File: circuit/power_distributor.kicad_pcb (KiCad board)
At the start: 4 copper layers, 210 x 100 mm, 199 parts, among them J1 UART, J10 AMASS XT60, J11 AMASS XT60, J12 AMASS XT60, J13 AMASS XT60, J14 AMASS XT60, J15 AMASS XT60, J16 AMASS XT60, J17 AMASS XT60, J18 AMASS XT60, J19 USB_B_Mini, J2 Opto_AUX, J3 AMASS XT60, J4 AMASS XT60, J5 AMASS XT60, J6 AMASS XT60, J7 AMASS XT60, J8 AMASS XT60, J9 AMASS XT60, Q1 AUIRFS8409-7P, Q2 IPB009N03LG, Q3 IPB009N03L_G, Q4 AUIRFS8409-7P, Q5 AUIRFS8409-7P, Q6 AUIRFS8409-7P, U1 UWE-12-10-Q12PB-C, U10 FT230XS, U11 MIC5504-3.3YM5, U12 74AHC595D, U13 PS2801C-4, U14 PS2801C-4, U15 LM5060, U16 LM5060, U17 LM5060, U2 UWE-12-10-Q12PB-C, U3 UEI30-050-Q12P-C, U4 TMR_6-2415WI, U5 i6A4W020A033V-001-R, U6 i6A4W020A033V-001-R, U7 LM5060, U8 LM5050-1, U9 LM5050-1

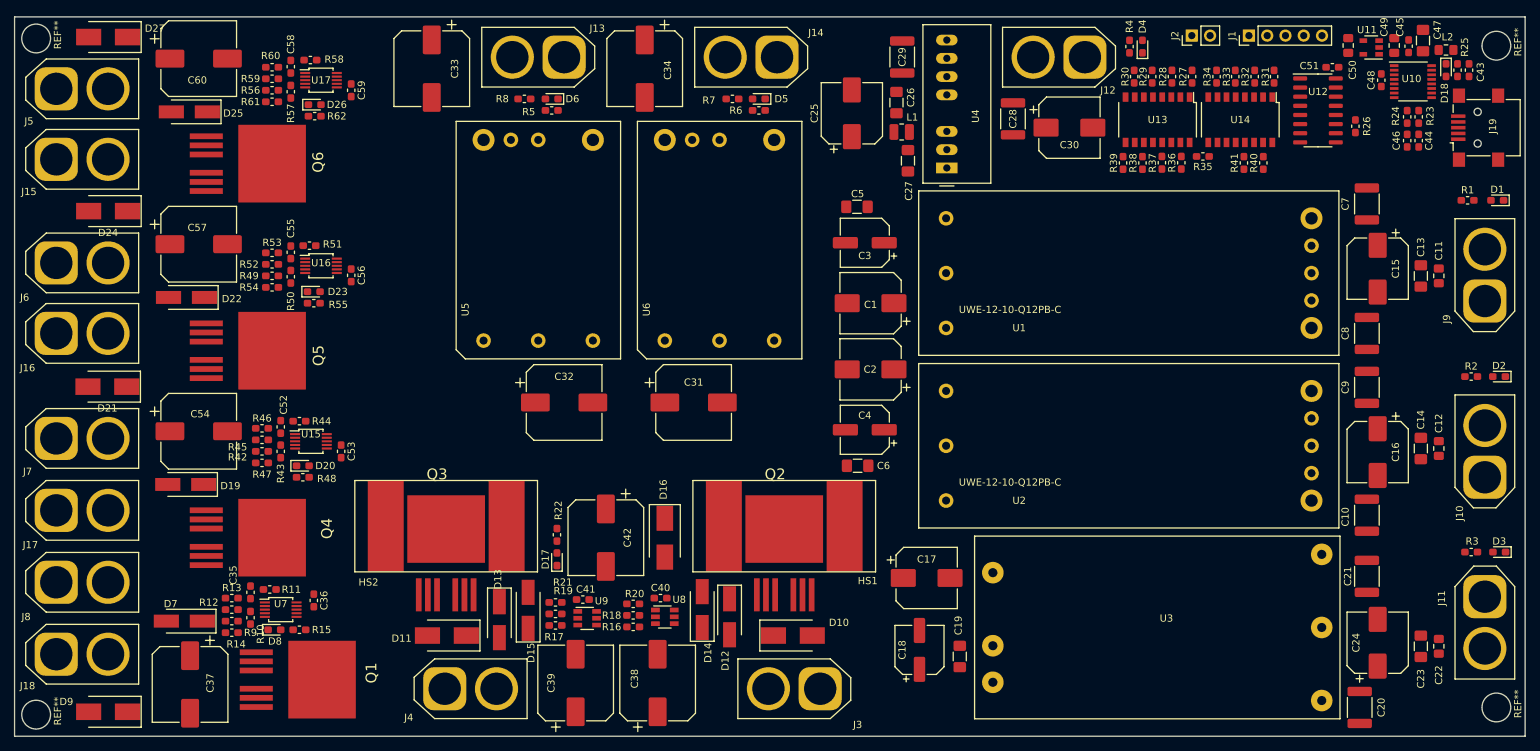
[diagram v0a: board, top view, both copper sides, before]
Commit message: Place all electrical planes and plane vias
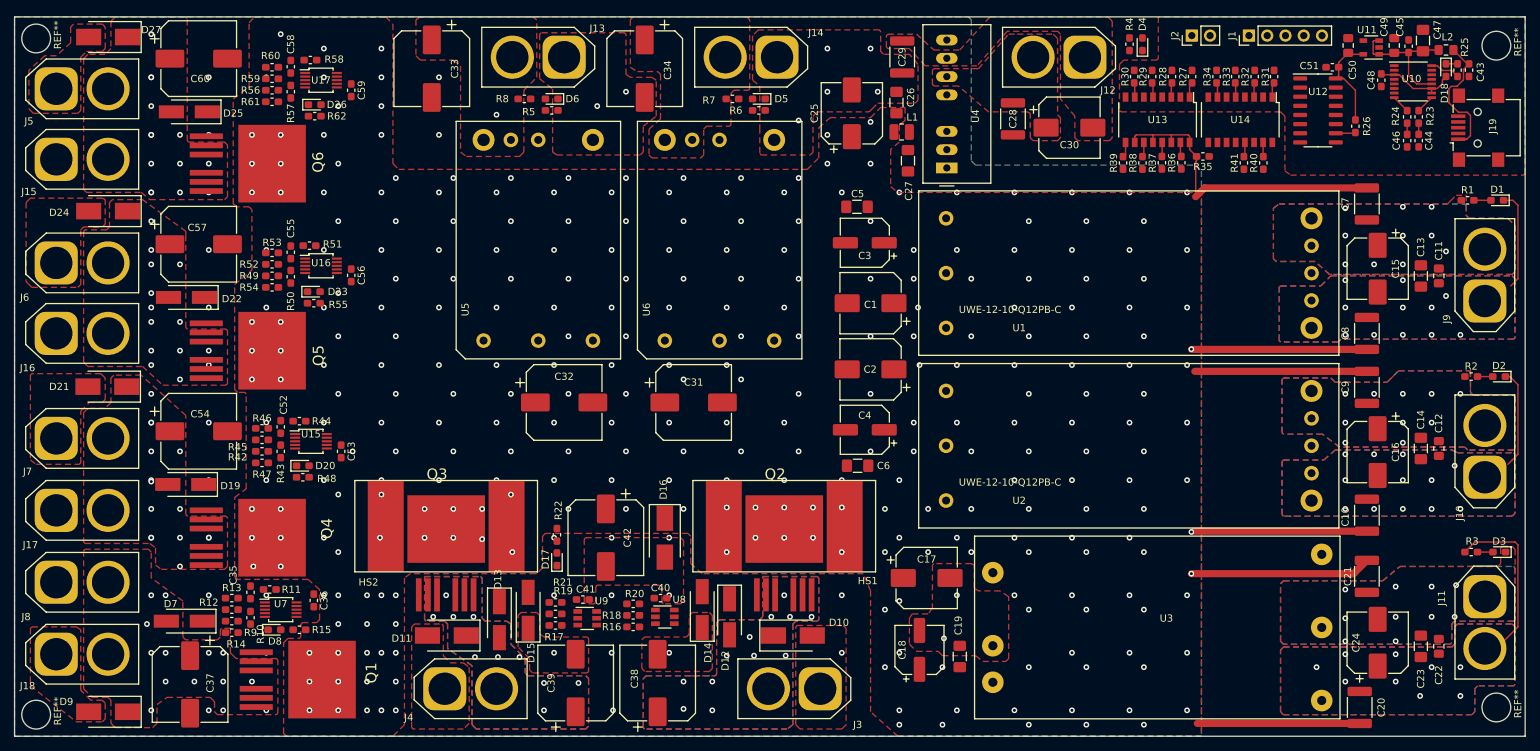
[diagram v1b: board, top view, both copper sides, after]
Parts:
- moved D4 0.33 mm to (201.8, 53.4)
- moved R4 0.33 mm to (200.0, 53.4)
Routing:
- net /Battery_ORing/+BATT: track 0.00 -> 90.2 mm, vias 0 -> 44
- net GNDPWR: track 0.00 -> 74.0 mm, vias 0 -> 147
- net /DC/DC_conveters/+5V_ISOLATED: track 0.00 -> 25.4 mm, vias 0 -> 9
- net VBUS: track 0.00 -> 18.9 mm
- net Net-(C43-Pad1): track 0.00 -> 18.4 mm
- net Net-(C50-Pad1): track 0.00 -> 14.0 mm
- net /DC/DC_conveters/GND_12V_ISOLATED_1: track 0.00 -> 13.9 mm, vias 0 -> 11
- net /DC/DC_conveters/GND_12V_ISOLATED_2: track 0.00 -> 13.9 mm, vias 0 -> 12
- net /USB_Interface/VCCIO: track 0.00 -> 11.4 mm
- net Net-(R25-Pad1): track 0.00 -> 4.22 mm
- net Net-(R26-Pad1): track 0.00 -> 2.77 mm
- net /USB_Interface/D_M: track 0.00 -> 2.55 mm
- net /USB_Interface/D_P: track 0.00 -> 2.55 mm
- net Net-(D1-Pad2): track 0.00 -> 2.38 mm
- net Net-(D3-Pad2): track 0.00 -> 2.15 mm
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- added copper zone on F.Cu, net /Battery_ORing/+BATT
- added copper zone on In1.Cu, net /Battery_ORing/+BATT
- added copper zone on B.Cu, net /Battery_ORing/+BATT_1
- added copper zone on F.Cu, net /Battery_ORing/+BATT_1
- added copper zone on In1.Cu, net /Battery_ORing/+BATT_1
- added copper zone on In2.Cu, net /Battery_ORing/+BATT_1
- added copper zone on B.Cu, net /Battery_ORing/+BATT_2
- added copper zone on F.Cu, net /Battery_ORing/+BATT_2
- added copper zone on In1.Cu, net /Battery_ORing/+BATT_2
- added copper zone on In2.Cu, net /Battery_ORing/+BATT_2
- added copper zone on B.Cu, net /DC/DC_conveters/+12V_ISOLATED_1
- added copper zone on F.Cu, net /DC/DC_conveters/+12V_ISOLATED_1
- added copper zone on In1.Cu, net /DC/DC_conveters/+12V_ISOLATED_1
- added copper zone on In2.Cu, net /DC/DC_conveters/+12V_ISOLATED_1
- added copper zone on B.Cu, net /DC/DC_conveters/+12V_ISOLATED_2
- added copper zone on F.Cu, net /DC/DC_conveters/+12V_ISOLATED_2
- added copper zone on In1.Cu, net /DC/DC_conveters/+12V_ISOLATED_2
- added copper zone on In2.Cu, net /DC/DC_conveters/+12V_ISOLATED_2
- added copper zone on F.Cu, net /DC/DC_conveters/+24V_ISOLATED
- added copper zone on B.Cu, net /DC/DC_conveters/+5V_ISOLATED
- added copper zone on F.Cu, net /DC/DC_conveters/+5V_ISOLATED
- added copper zone on In1.Cu, net /DC/DC_conveters/+5V_ISOLATED
- added copper zone on In2.Cu, net /DC/DC_conveters/+5V_ISOLATED
- added copper zone on F.Cu, net /DC/DC_conveters/+8.4V_1
- added copper zone on In1.Cu, net /DC/DC_conveters/+8.4V_1
- added copper zone on F.Cu, net /DC/DC_conveters/+8.4V_2
- added copper zone on In1.Cu, net /DC/DC_conveters/+8.4V_2
- added copper zone on B.Cu, net /DC/DC_conveters/GND_12V_ISOLATED_1
- added copper zone on F.Cu, net /DC/DC_conveters/GND_12V_ISOLATED_1
- added copper zone on In1.Cu, net /DC/DC_conveters/GND_12V_ISOLATED_1
- added copper zone on In2.Cu, net /DC/DC_conveters/GND_12V_ISOLATED_1
- added copper zone on B.Cu, net /DC/DC_conveters/GND_12V_ISOLATED_2
- added copper zone on F.Cu, net /DC/DC_conveters/GND_12V_ISOLATED_2
- added copper zone on In1.Cu, net /DC/DC_conveters/GND_12V_ISOLATED_2
- added copper zone on In2.Cu, net /DC/DC_conveters/GND_12V_ISOLATED_2
- added copper zone on F.Cu, net /DC/DC_conveters/GND_24V_ISOLATED
- added copper zone on B.Cu, net /DC/DC_conveters/GND_5V_ISOLATED
- added copper zone on F.Cu, net /DC/DC_conveters/GND_5V_ISOLATED
- added copper zone on In1.Cu, net /DC/DC_conveters/GND_5V_ISOLATED
- added copper zone on In2.Cu, net /DC/DC_conveters/GND_5V_ISOLATED
- added copper zone on F.Cu, net /Thruster_Switch_1/+Vout
- added copper zone on In1.Cu, net /Thruster_Switch_1/+Vout
- added copper zone on F.Cu, net /Thruster_Switch_2/+Vout
- added copper zone on In1.Cu, net /Thruster_Switch_2/+Vout
- added copper zone on F.Cu, net /Thruster_Switch_3/+Vout
- added copper zone on In1.Cu, net /Thruster_Switch_3/+Vout
- added copper zone on F.Cu, net /Thruster_Switch_4/+Vout
- added copper zone on In1.Cu, net /Thruster_Switch_4/+Vout
- added copper zone on F.Cu, net GND
- added copper zone on B.Cu, net GNDPWR
- added copper zone on F.Cu, net GNDPWR
- added copper zone on In1.Cu, net GNDPWR
- added copper zone on In2.Cu, net GNDPWR

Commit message: Complete all PCB routing.
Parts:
- moved R17 5.00 mm to (125.2, 134.2), turned to 180 degrees
- moved R19 5.00 mm to (125.2, 132.6), turned to 180 degrees
- moved R21 5.00 mm to (125.2, 131.0), turned to 180 degrees
- moved C41 3.41 mm to (120.6, 130.4), turned to 180 degrees
- moved U9 3.41 mm to (121.2, 133.0)
- moved U8 0.40 mm to (135.4, 133.4)
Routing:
- net /Thruster_Switch_4/EN: track 2.12 -> 174.6 mm, vias 0 -> 2
- net /Thruster_Switch_3/EN: track 2.05 -> 150.1 mm, vias 0 -> 2
- net /Thruster_Switch_1/EN: track 2.00 -> 139.9 mm, vias 0 -> 2
- net /Thruster_Switch_2/EN: track 1.97 -> 128.1 mm, vias 0 -> 2
- net /DC/DC_conveters/EN_8.4V: track 0.00 -> 124.3 mm, vias 0 -> 1
- net GNDPWR: track 74.0 -> 174.5 mm, vias 147 -> 194
- net /DC/DC_conveters/EN_5V: track 2.03 -> 99.5 mm, vias 0 -> 1
- net /DC/DC_conveters/EN_12V: track 1.99 -> 87.7 mm, vias 0 -> 1
- net /Battery_ORing/+BATT: track 90.2 -> 138.6 mm
- net /USB_Interface/OPTO_E: track 0.00 -> 41.9 mm, vias 0 -> 1
- net /USB_Interface/OPTO_C: track 0.00 -> 37.4 mm, vias 0 -> 1
- net Net-(D13-Pad1): track 0.00 -> 30.6 mm
- net Net-(R30-Pad2): track 0.00 -> 27.7 mm, vias 0 -> 2
- net Net-(R34-Pad2): track 0.00 -> 26.7 mm
- net /USB_Interface/~CTS: track 0.00 -> 26.7 mm, vias 0 -> 1
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- added copper zone on B.Cu, net GND

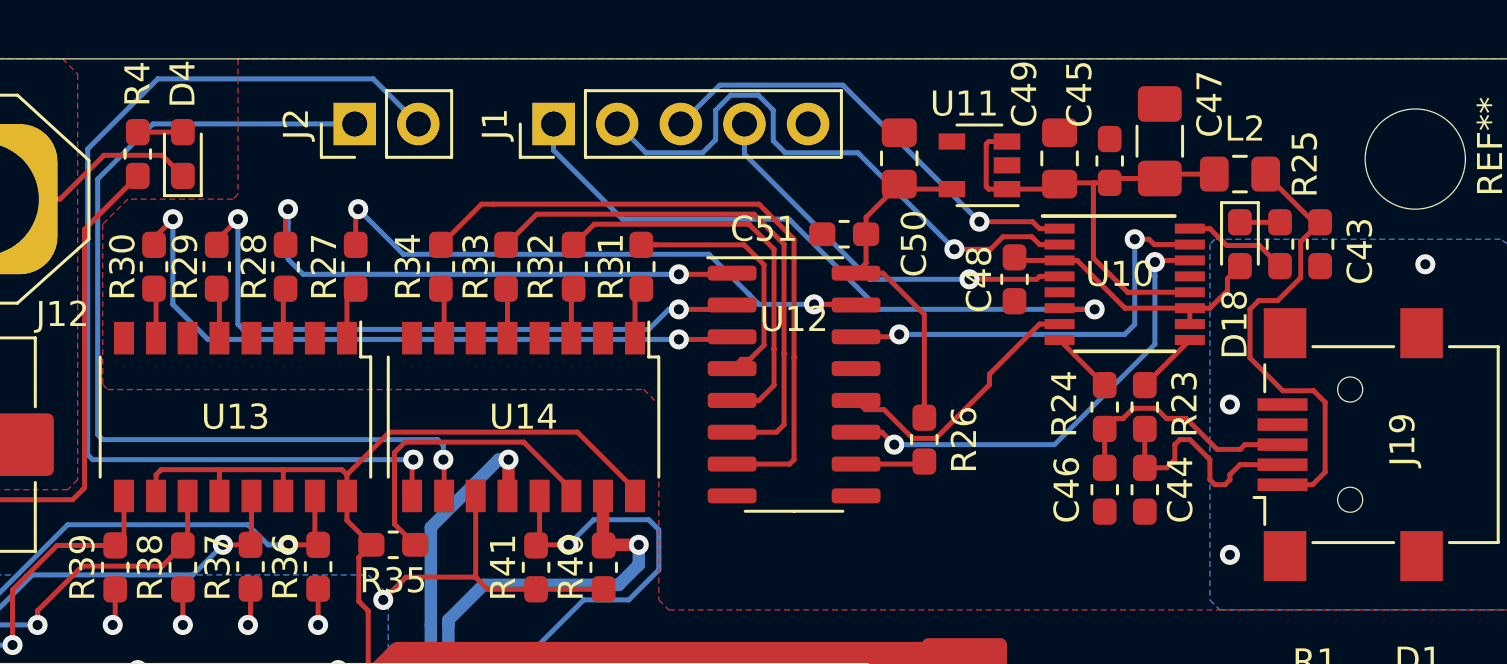
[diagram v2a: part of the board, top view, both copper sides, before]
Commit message: Add VBUS output to RS232 connector
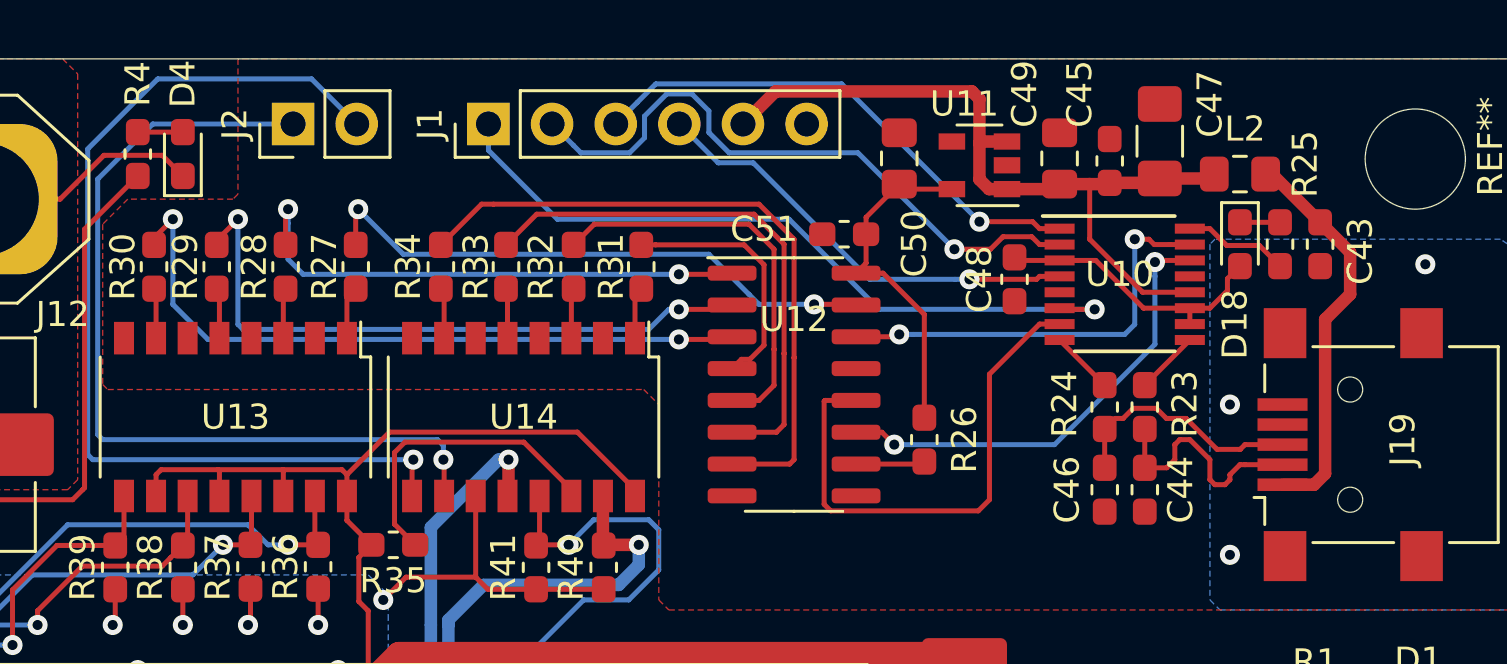
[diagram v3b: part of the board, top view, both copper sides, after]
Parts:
- J1: footprint Connector_PinHeader_2.54mm:PinHeader_1x05_P2.54mm_Vertical -> Connector_PinHeader_2.54mm:PinHeader_1x06_P2.54mm_Vertical
- moved J1 2.60 mm to (214.0, 52.2)
- moved J2 2.46 mm to (206.2, 52.2)
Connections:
- J1 pad 5: GND -> VBUS
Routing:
- net VBUS: track 19.4 -> 31.9 mm
- net Net-(U10-Pad7): track 10.9 -> 20.9 mm
- net /USB_Interface/TXD: track 18.1 -> 20.8 mm
- net /USB_Interface/~CTS: track 26.7 -> 29.3 mm
- net /USB_Interface/OPTO_C: track 37.4 -> 34.9 mm
- net /USB_Interface/OPTO_E: track 41.9 -> 39.4 mm
- net Net-(C43-Pad1): track 18.4 -> 16.1 mm
- net /USB_Interface/~RTS: track 23.4 -> 25.6 mm
- net /USB_Interface/RXD: track 15.9 -> 17.8 mm

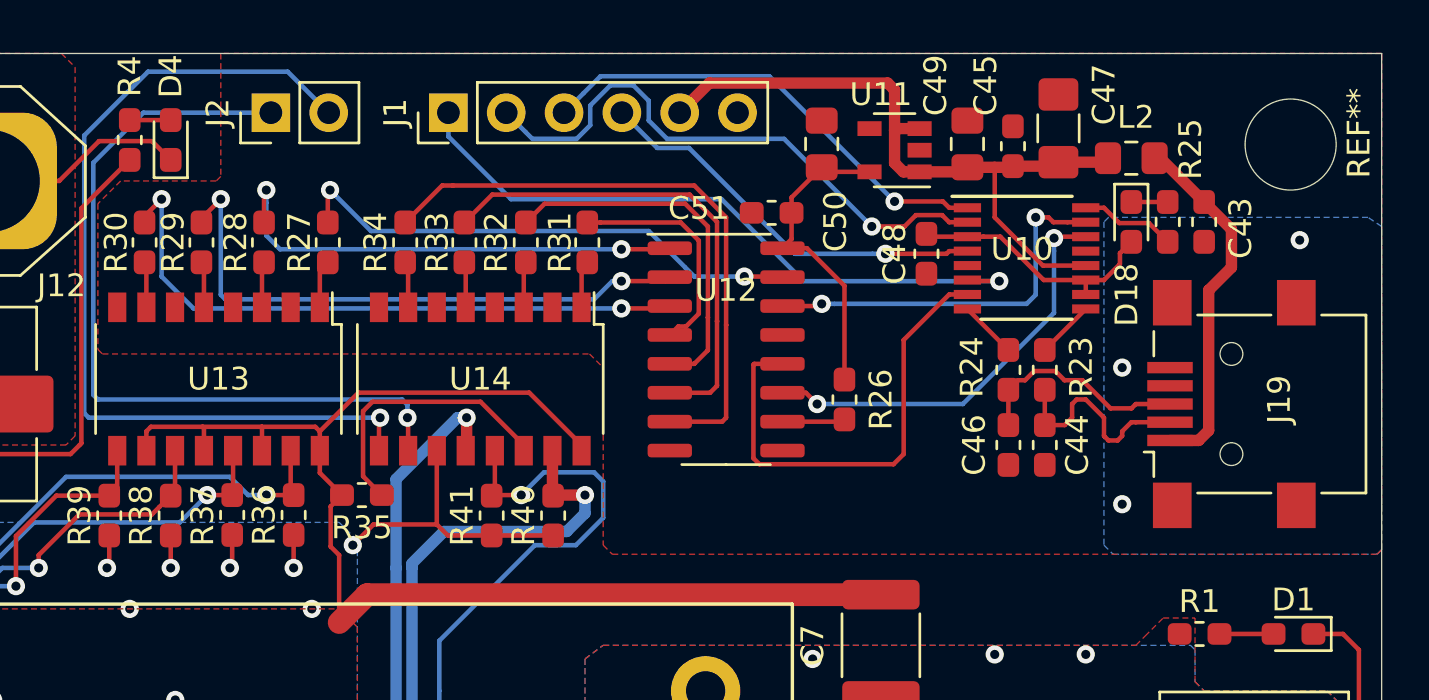
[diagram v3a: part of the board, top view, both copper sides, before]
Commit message: Change LDO to LM1117-3.3
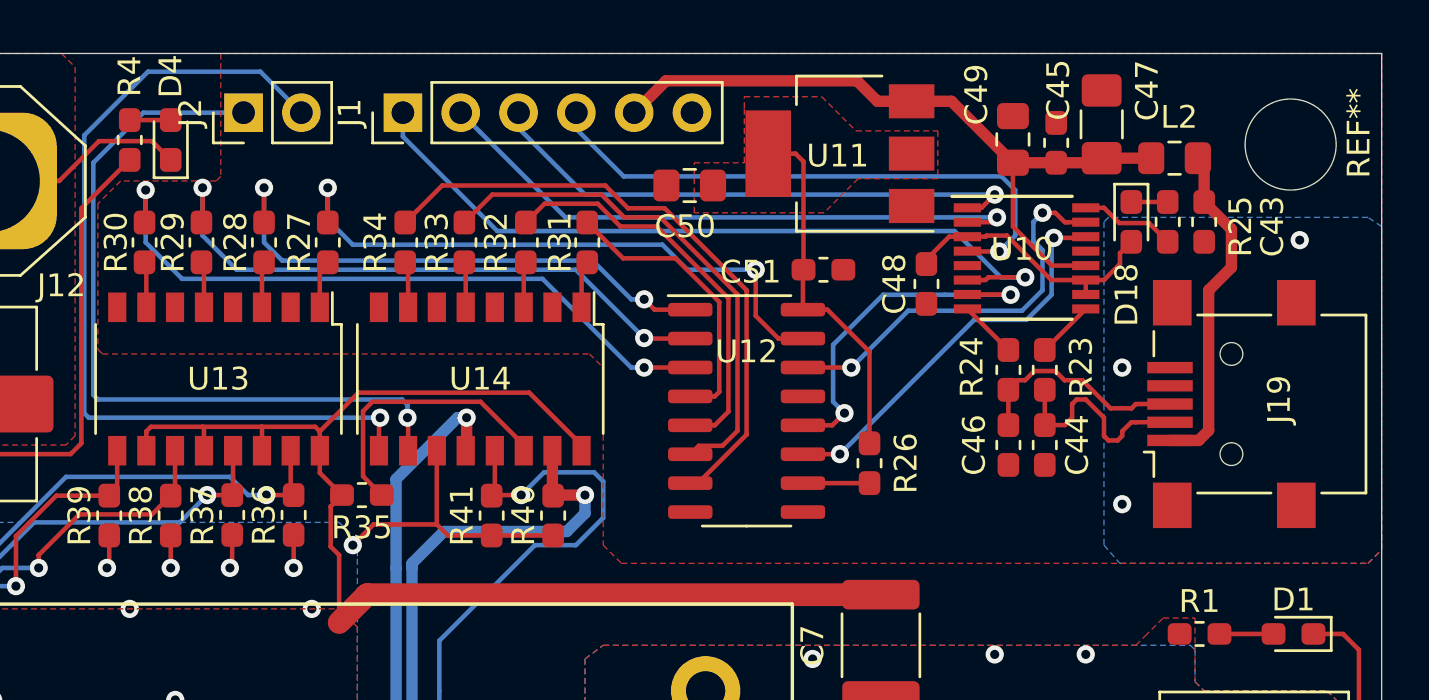
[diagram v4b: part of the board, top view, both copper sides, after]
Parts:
- U11: value MIC5504-3.3YM5 -> LM1117-3.3; footprint Package_TO_SOT_SMD:SOT-23-5 -> Package_TO_SOT_SMD:SOT-223-3_TabPin2
- moved C50 6.08 mm to (224.6, 55.4), turned to 180 degrees
- moved C51 3.38 mm to (230.5, 59.1), turned to 0 degrees
- moved R26 3.01 mm to (232.5, 67.6)
- moved U12 2.85 mm to (227.1, 65.3)
- moved U11 2.40 mm to (231.2, 54.0)
- moved C49 2.01 mm to (238.8, 53.4)
- moved J1 2.00 mm to (212.0, 52.2)
- moved C47 1.91 mm to (242.7, 52.7)
- moved C45 1.91 mm to (240.7, 53.5)
- moved L2 1.90 mm to (245.9, 54.2)
- moved C48 1.33 mm to (235.0, 59.7)
- moved J2 1.20 mm to (205.0, 52.2)
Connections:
- U11 pad 1: VBUS -> GND
- U11 pad 2: GND -> Net-(C50-Pad1)
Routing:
- net /USB_Interface/RXD: track 17.8 -> 25.7 mm
- net Net-(U10-Pad7): track 20.9 -> 15.9 mm, vias 0 -> 2
- net /USB_Interface/~CTS: track 29.3 -> 33.5 mm
- net Net-(R27-Pad2): track 22.9 -> 27.2 mm
- net /USB_Interface/TXD: track 20.8 -> 24.2 mm
- net Net-(R31-Pad2): track 10.1 -> 12.6 mm
- net Net-(R28-Pad2): track 21.5 -> 23.9 mm
- net Net-(R30-Pad2): track 27.7 -> 30.0 mm
- net Net-(C50-Pad1): track 14.0 -> 15.9 mm
- net Net-(R32-Pad2): track 16.1 -> 17.9 mm
- net Net-(R33-Pad2): track 21.5 -> 22.8 mm
- net /USB_Interface/~RTS: track 25.6 -> 26.9 mm
- net /USB_Interface/OPTO_E: track 39.4 -> 38.2 mm
- net /USB_Interface/OPTO_C: track 34.9 -> 33.7 mm
- net Net-(R29-Pad2): track 25.8 -> 26.9 mm
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- added copper zone on F.Cu, net Net-(C50-Pad1)
